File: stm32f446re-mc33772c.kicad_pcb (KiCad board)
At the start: 4 copper layers, 105.3 x 62.5 mm, 120 parts, among them J1 Conn_01x02, J2 USB_B_Micro, J3 Conn_01x03, J4 Conn_01x03, J5 S7B-XH-A, J6 SM06B-GHS-TB, U1 STM32F446RETx, U2 MC33772CTP1AE, U3 LD1086D2M33TR, U4 AMS1117-3.3, U6 LMR51450SDRRR, U7 SN65HVD232, Y1 16MHz

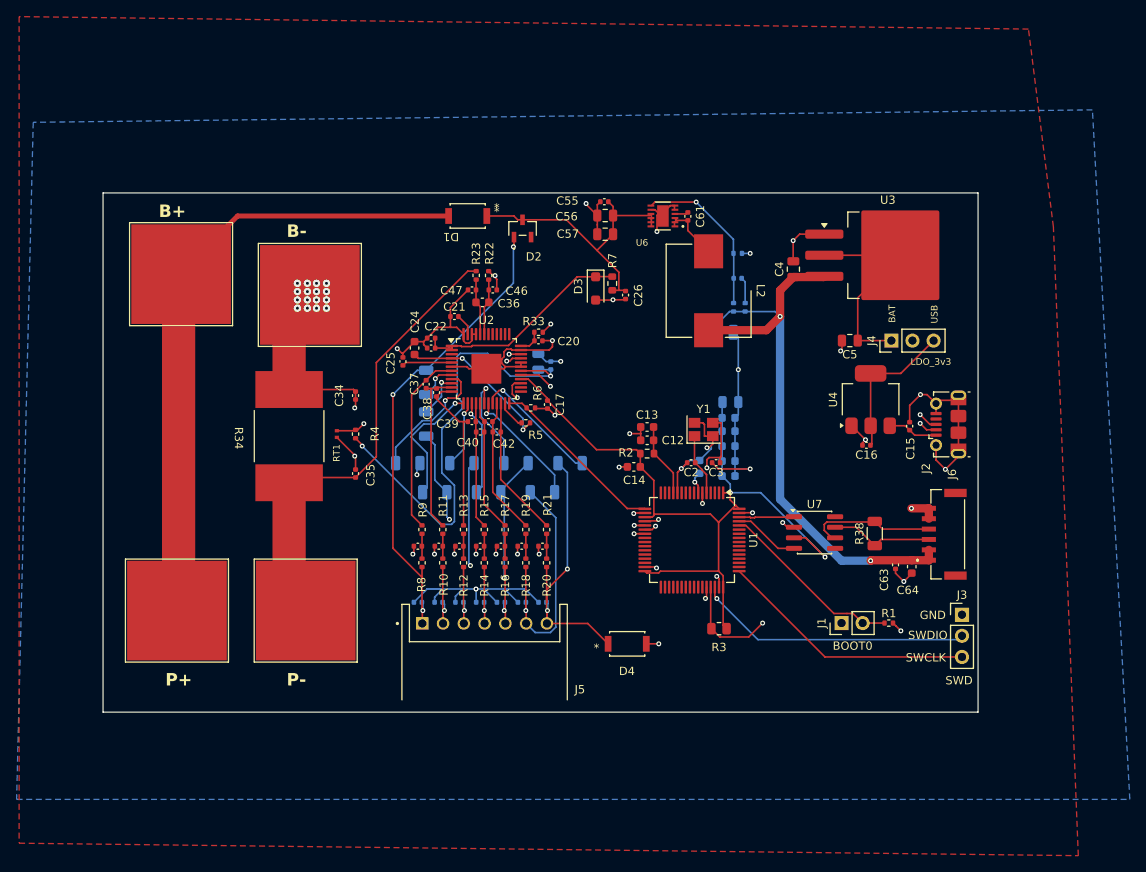
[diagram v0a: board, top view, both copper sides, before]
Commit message: update 3D model
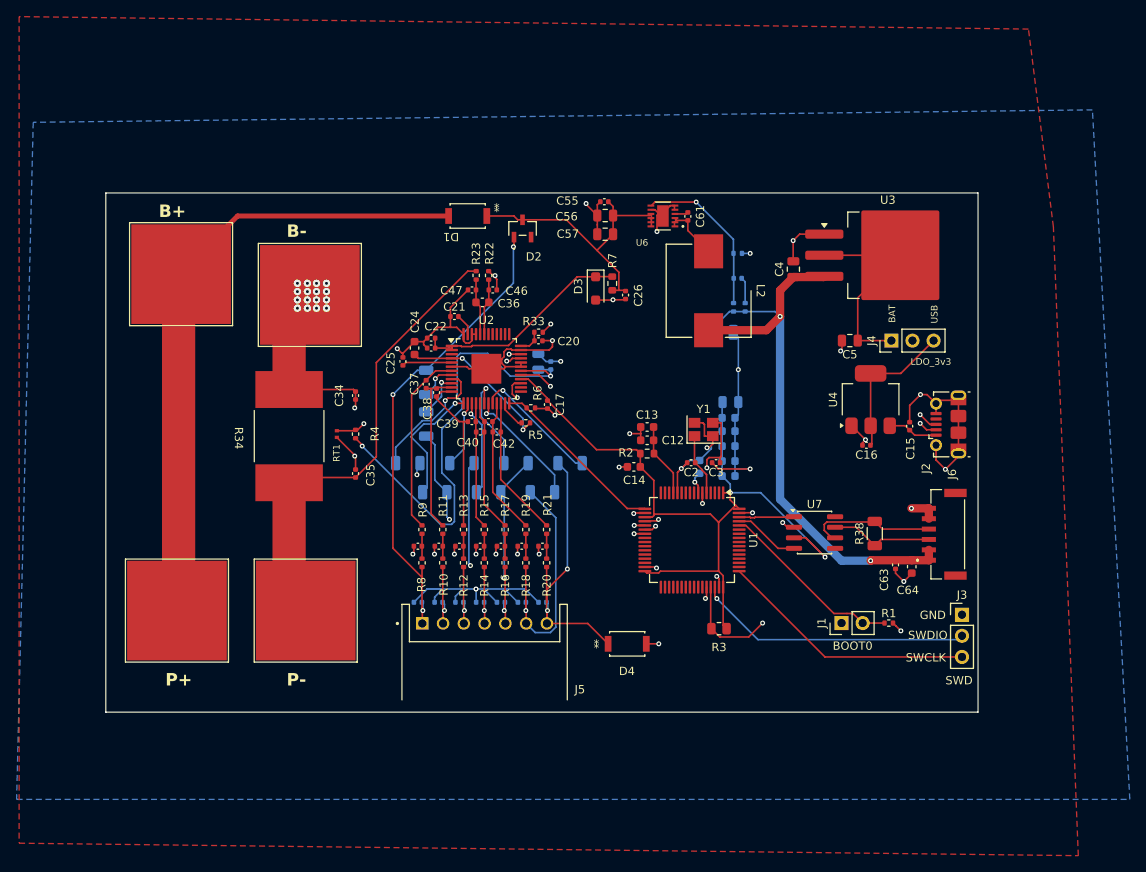
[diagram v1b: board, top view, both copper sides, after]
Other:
- board size 105.3 x 62.5 mm -> 105 x 62.5 mm
- board text removed: "*"
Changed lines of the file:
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@@
 			(outputformat 1)
 			(mirror no)
-			(drillshape 1)
+			(drillshape 0)
 			(scaleselection 1)
-			(outputdirectory "")
+			(outputdirectory "DRL/")
 		)
 	)
@@
 		(sheetname "/STM32F446RE/")
 		(sheetfile "stm32f446re-mc33772c.kicad_sch")
-		(units
-			(unit
-				(name "A")
-				(pins "SH" "5" "1" "3" "2" "4")
-			)
-		)
 		(attr smd)
 		(duplicate_pad_numbers_are_jumpers no)
@@
 		)
 		(embedded_fonts no)
-		(model "${KICAD10_3DMODEL_DIR}/Connector_USB.3dshapes/USB_Micro-B_Molex-105017-0001.step"
+		(model "${KIPRJMOD}/1050170001/1050170001.stp"
 			(offset
-				(xyz 0 0 0)
+				(xyz 0 -1 1)
 			)
 			(scale
@@
 			)
 			(rotate
-				(xyz 0 0 0)
+				(xyz -90 -0 -0)
 			)
 		)
@@
 		(sheetname "/STM32F446RE/")
 		(sheetfile "stm32f446re-mc33772c.kicad_sch")
-		(units
-			(unit
-				(name "A")
-				(pins "1" "2" "3" "4" "5" "6")
-			)
-		)
 		(attr smd)
 		(duplicate_pad_numbers_are_jumpers no)
@@
 		)
 		(embedded_fonts no)
+		(model "${KIPRJMOD}/SM06B_GHS_TB/SM06B-GHS-TB.step"
+			(offset
+				(xyz 0 0 0)
+			)
+			(scale
+				(xyz 1 1 1)
+			)
+			(rotate
+				(xyz -90 -0 -0)
+			)
+		)
 	)
 	(footprint "Capacitor_SMD:C_0402_1005Metric"
@@
 		(sheetname "/STM32F446RE/")
 		(sheetfile "stm32f446re-mc33772c.kicad_sch")
-		(units
-			(unit
-				(name "A")
-				(pins "10" "11" "12" "9" "6" "4" "1" "2" "3" "7" "5" "13" "8")
-			)
-		)
 		(attr smd)
 		(duplicate_pad_numbers_are_jumpers no)
@@
 		)
 		(embedded_fonts no)
+		(model "${KIPRJMOD}/LMR51450SDRRR/DRR0012G.stp"
+			(offset
+				(xyz 0 0 0)
+			)
+			(scale
+				(xyz 1 1 1)
+			)
+			(rotate
+				(xyz 0 0 0)
+			)
+		)
 	)
 	(footprint "MyFootLib:WSLP5931L1000FEA"
@@
 		(sheetname "/POWER/")
 		(sheetfile "power.kicad_sch")
-		(units
-			(unit
-				(name "A")
-				(pins "1" "2")
-			)
-		)
 		(attr smd)
 		(duplicate_pad_numbers_are_jumpers no)
@@
 		)
 		(embedded_fonts no)
+		(model "${KIPRJMOD}/WSLP5931L1000FEA/WSLP5931L1000FEA.step"
+			(offset
+				(xyz 0 0 0)
+			)
+			(scale
+				(xyz 1 1 1)
+			)
+			(rotate
+				(xyz 0 0 0)
+			)
+		)
 	)
 	(footprint "Package_TO_SOT_SMD:SOT-223-3_TabPin2"
@@
 		(sheetname "/POWER/")
 		(sheetfile "power.kicad_sch")
-		(units
-			(unit
-				(name "A")
-				(pins "2" "1")
-			)
-		)
 		(attr smd)
 		(duplicate_pad_numbers_are_jumpers no)
@@
 		)
 		(fp_text user "*"
+			(at -3.7 0 0)
+			(unlocked yes)
+			(layer "F.SilkS")
+			(effects
+				(font
+					(size 1 1)
+					(thickness 0.15)
+				)
+			)
+		)
+		(fp_text user "*"
+			(at -3.7 0.5 0)
+			(layer "F.SilkS")
+			(effects
+				(font
+					(size 1 1)
+					(thickness 0.15)
+				)
+			)
+		)
+		(fp_text user "*"
 			(at -1.7399 0 0)
 			(unlocked yes)
@@
 		)
 		(embedded_fonts no)
+		(model "${KIPRJMOD}/PMEG3050EP_115/SDO_CFP5_SOD128_NEX.iges"
+			(offset
+				(xyz 0 0 0)
+			)
+			(scale
+				(xyz 1 1 1)
+			)
+			(rotate
+				(xyz 0 0 0)
+			)
+		)
 	)
 	(footprint "Capacitor_SMD:C_0402_1005Metric"
@@
 		(sheetname "/POWER/")
 		(sheetfile "power.kicad_sch")
-		(units
-			(unit
-				(name "A")
-				(pins "1" "2" "3" "4" "5" "6" "7")
-			)
-		)
 		(attr through_hole)
 		(duplicate_pad_numbers_are_jumpers no)
@@
 		)
 		(embedded_fonts no)
+		(model "${KIPRJMOD}/S7B_XH_A/S7B-XH-A.step"
+			(offset
+				(xyz 0 0 0)
+			)
+			(scale
+				(xyz 1 1 1)
+			)
+			(rotate
+				(xyz -90 -0 -0)
+			)
+		)
 	)
 	(footprint "Resistor_SMD:R_0402_1005Metric"
@@
 		(sheetname "/POWER/")
 		(sheetfile "power.kicad_sch")
-		(units
-			(unit
-				(name "A")
-				(pins "2" "1")
-			)
-		)
 		(attr smd)
 		(duplicate_pad_numbers_are_jumpers no)
@@
 		)
 		(embedded_fonts no)
+		(model "${KIPRJMOD}/PMEG3050EP_115/SDO_CFP5_SOD128_NEX.iges"
+			(offset
+				(xyz 0 0 0)
+			)
+			(scale
+				(xyz 1 1 1)
+			)
+			(rotate
+				(xyz 0 0 0)
+			)
+		)
 	)
 	(footprint "MyFootLib:L_Wurth_WE-LHMI-1040"
@@
 	)
 	(gr_rect
-		(start 115.1 41.725)
+		(start 115.431914 41.725)
 		(end 220.431914 104.225)
 		(stroke
@@
 		)
 	)
-	(gr_text "*"
-		(at 174.5 96.5 0)
-		(layer "F.SilkS")
-		(effects
-			(font
-				(size 1 1)
-				(thickness 0.15)
-			)
-		)
-	)

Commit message: feat: change B+/P+ to B.Cu and onto one pad
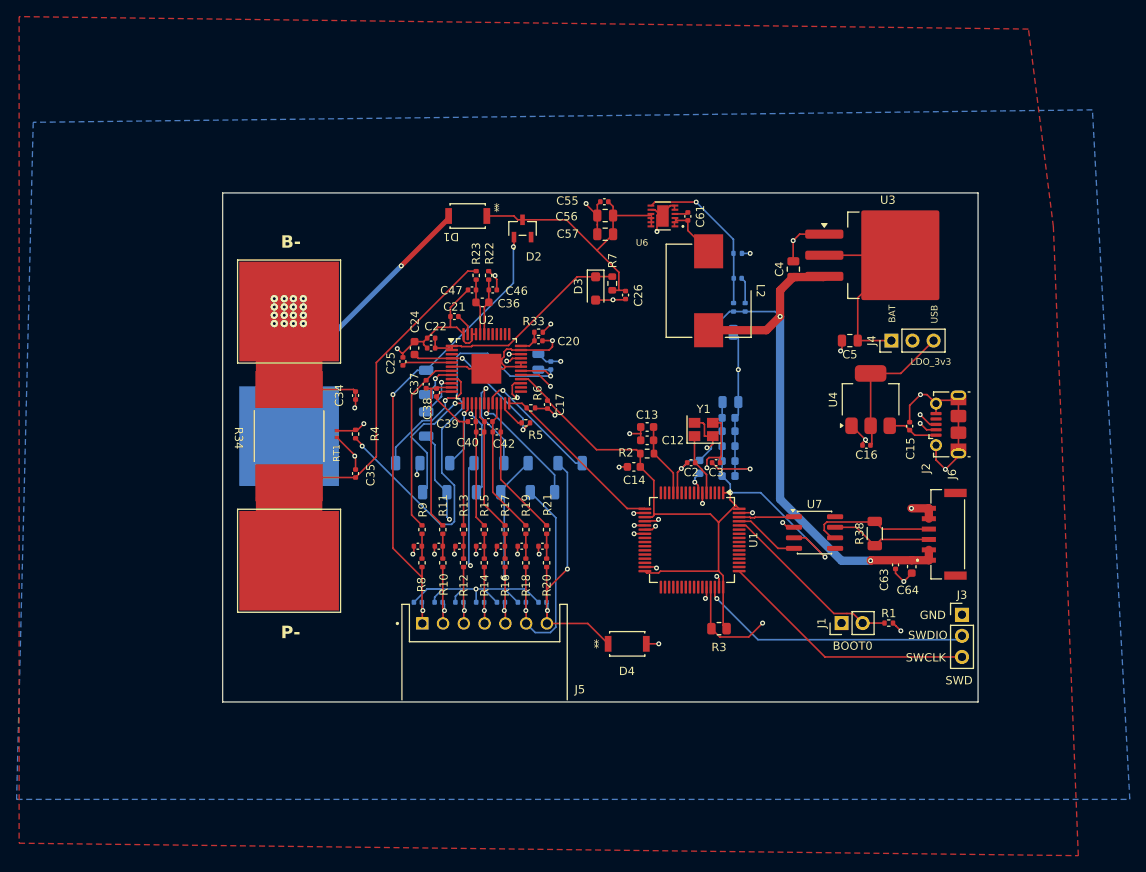
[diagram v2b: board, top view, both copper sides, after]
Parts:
- removed PAD2: pad, MyFootLib:INPUT_PAD
- PAD1: moved to B.Cu
- moved PAD1 23.4 mm to (137.5, 71.0), turned to 180 degrees
- moved PAD4 6.32 mm to (137.5, 86.0)
- moved PAD3 3.20 mm to (137.5, 56.0)
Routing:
- net Pack_24V: track 76.2 -> 34.5 mm, vias 0 -> 1
- net Pack-: track 55.9 -> 42.2 mm
- net Rsense_P: track 220.0 -> 210.1 mm
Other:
- board size 105 x 62.5 mm -> 90.9 x 61.3 mm

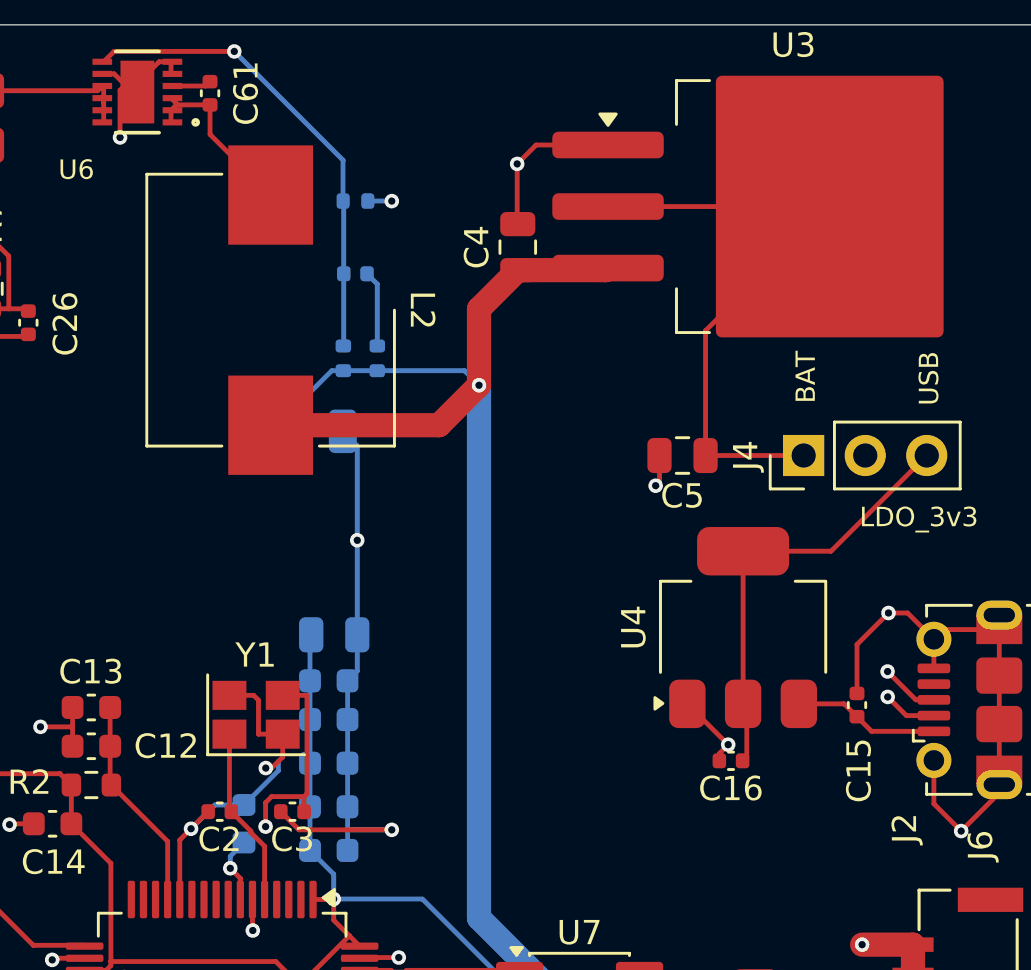
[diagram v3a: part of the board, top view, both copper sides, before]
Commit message: update for JLCPCB with LCSC part #
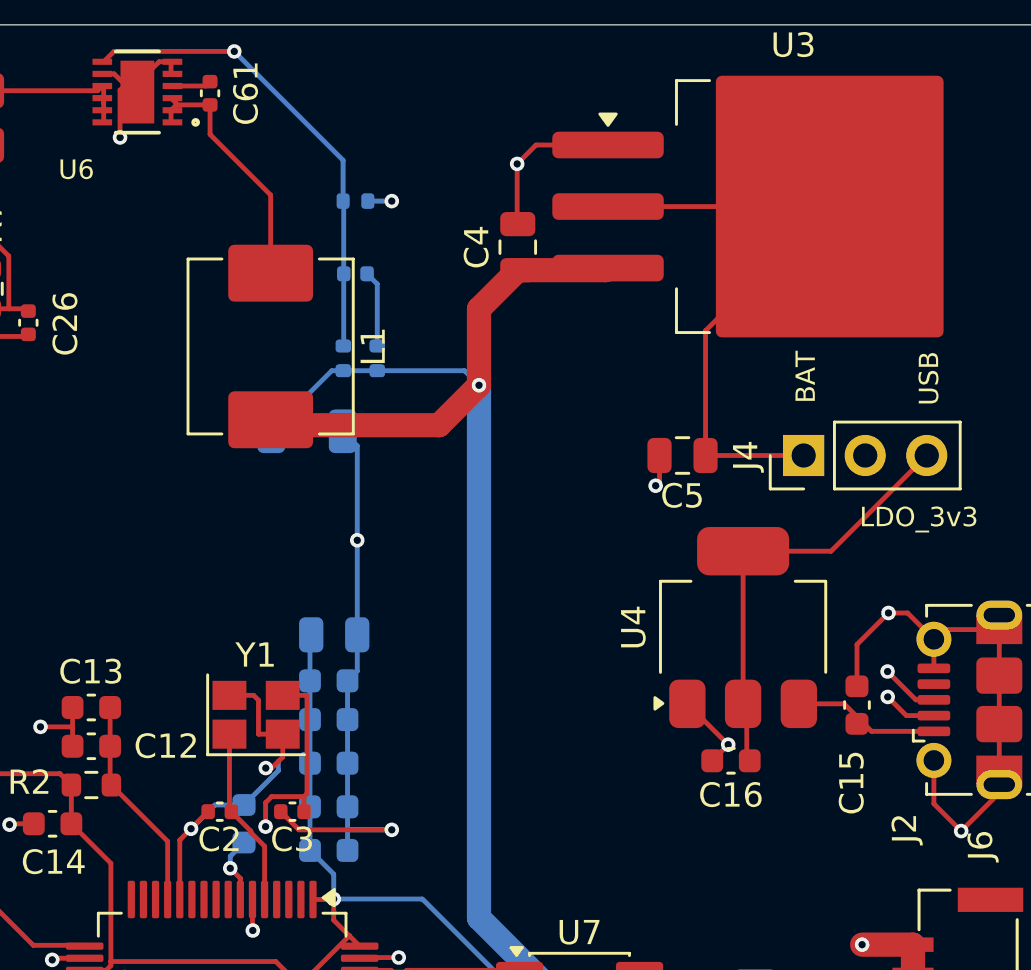
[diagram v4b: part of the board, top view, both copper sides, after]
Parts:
- removed L2: 1040_74437368033, MyFootLib:L_Wurth_WE-LHMI-1040
- added L1: 3.3uH, MyFootLib:PSPMAA0605H-3R3M-ANP, F.Cu at (188.0, 55.0)
- C10, C11, C58, C7, C8, C9: value 100.0n -> 100n
- C15, C16: footprint Capacitor_SMD:C_0402_1005Metric -> Capacitor_SMD:C_0603_1608Metric
- C6: value 10.0u -> 10u
- D3: value BZT52-B39_R1_00001 -> BZT52-C39_R1_00001
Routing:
- net Net-(U6-SW): track 7.33 -> 10.6 mm

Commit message: update PCB for jlcpcb toolkit
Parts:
- C2, C3: value 18p -> 8p
- U1: value STM32F446RETx -> STM32F446RET6

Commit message: export to JLCPCB
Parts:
- C17, C18, C27, C28, C29, C30, C31, C32, C33, C61: value 0.1u -> 100n
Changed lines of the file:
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@@
 			)
 		)
+		(property "FT Rotation Offset" "90"
+			(at 0 0 90)
+			(unlocked yes)
+			(layer "F.Fab")
+			(hide yes)
+			(effects
+				(font
+					(size 1 1)
+					(thickness 0.15)
+				)
+			)
+		)
 		(property ki_fp_filters "Connector*:*_1x??_*")
 		(sheetname "/STM32F446RE/")
@@
 			)
 		)
+		(property "FT Rotation Offset" "90"
+			(at 0 0 90)
+			(unlocked yes)
+			(layer "F.Fab")
+			(hide yes)
+			(effects
+				(font
+					(size 1 1)
+					(thickness 0.15)
+				)
+			)
+		)
 		(property ki_fp_filters "Connector*:*_1x??_*")
 		(sheetname "/STM32F446RE/")
@@
 			)
 		)
-		(property "Value" "0.1u"
+		(property "Value" "100n"
 			(at 0 1.16 0)
 			(layer "F.Fab")
@@
 			)
 		)
+		(property "FT Rotation Offset" "0"
+			(at 0 0 270)
+			(unlocked yes)
+			(layer "F.Fab")
+			(hide yes)
+			(effects
+				(font
+					(size 1 1)
+					(thickness 0.15)
+				)
+			)
+		)
 		(property ki_fp_filters "D?SOD?123F*")
 		(sheetname "/POWER/")
@@
 			)
 		)
-		(property "Value" "0.1u"
+		(property "Value" "100n"
 			(at 0 1.16 0)
 			(layer "F.Fab")
@@
 			)
 		)
-		(property "Value" "0.1u"
+		(property "Value" "100n"
 			(at 0 1.16 0)
 			(layer "F.Fab")
@@
 			)
 		)
-		(property "Value" "0.1u"
+		(property "Value" "100n"
 			(at 0 1.16 0)
 			(layer "F.Fab")
@@
 			)
 		)
+		(property "FT Rotation Offset" "-90"
+			(at 0 0 0)
+			(unlocked yes)
+			(layer "F.Fab")
+			(hide yes)
+			(effects
+				(font
+					(size 1 1)
+					(thickness 0.15)
+				)
+			)
+		)
 		(property ki_fp_filters "SOT-23-3_1P4X3P040_ONS SOT-23-3_1P4X3P040_ONS-M SOT-23-3_1P4X3P040_ONS-L")
 		(sheetname "/POWER/")
@@
 			)
 		)
+		(property "FT Rotation Offset" "90"
+			(at 0 0 0)
+			(unlocked yes)
+			(layer "F.Fab")
+			(hide yes)
+			(effects
+				(font
+					(size 1 1)
+					(thickness 0.15)
+				)
+			)
+		)
 		(property ki_fp_filters "Connector*:*_1x??_*")
 		(sheetname "/STM32F446RE/")
@@
 			)
 		)
+		(property "FT Rotation Offset" "0"
+			(at 0 0 0)
+			(unlocked yes)
+			(layer "F.Fab")
+			(hide yes)
+			(effects
+				(font
+					(size 1 1)
+					(thickness 0.15)
+				)
+			)
+		)
 		(property ki_fp_filters "SDO_CFP5_SOD128_NEX SDO_CFP5_SOD128_NEX-M SDO_CFP5_SOD128_NEX-L")
 		(sheetname "/POWER/")
@@
 			)
 		)
-		(property "Value" "0.1u"
+		(property "Value" "100n"
 			(at 0 1.16 0)
 			(layer "F.Fab")
@@
 			)
 		)
+		(property "FT Rotation Offset" "180"
+			(at 0 0 0)
+			(unlocked yes)
+			(layer "F.Fab")
+			(hide yes)
+			(effects
+				(font
+					(size 1 1)
+					(thickness 0.15)
+				)
+			)
+		)
 		(sheetname "/POWER/")
 		(sheetfile "power.kicad_sch")
@@
 			)
 		)
-		(property "Value" "0.1u"
+		(property "Value" "100n"
 			(at 0 1.16 0)
 			(layer "F.Fab")
@@
 			)
 		)
-		(property "Value" "0.1u"
+		(property "Value" "100n"
 			(at 0 1.16 90)
 			(layer "F.Fab")
@@
 			)
 		)
-		(property "Value" "0.1u"
+		(property "Value" "100n"
 			(at 0 1.16 90)
 			(layer "F.Fab")
@@
 			)
 		)
+		(property "FT Rotation Offset" "0"
+			(at 0 0 180)
+			(unlocked yes)
+			(layer "F.Fab")
+			(hide yes)
+			(effects
+				(font
+					(size 1 1)
+					(thickness 0.15)
+				)
+			)
+		)
 		(property ki_fp_filters "SDO_CFP5_SOD128_NEX SDO_CFP5_SOD128_NEX-M SDO_CFP5_SOD128_NEX-L")
 		(sheetname "/POWER/")
@@
 			)
 		)
-		(property "Value" "0.1u"
+		(property "Value" "100n"
 			(at 0 1.16 0)
 			(layer "F.Fab")
@@
 			)
 		)
-		(property "Value" "0.1u"
+		(property "Value" "100n"
 			(at 0 -1.16 90)
 			(layer "B.Fab")

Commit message: add testpoint
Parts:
- added TP1: TP_SPI_NSS, TestPoint:TestPoint_Pad_D1.0mm, F.Cu at (174.5, 80.0)
- added TP2: TP_SPI_SCK, TestPoint:TestPoint_Pad_D1.0mm, F.Cu at (174.5, 83.6)
- added TP3: TP_SPI_MISO, TestPoint:TestPoint_Pad_D1.0mm, F.Cu at (174.5, 86.6)
- added TP4: TP_SPI_MOSI, TestPoint:TestPoint_Pad_D1.0mm, F.Cu at (174.5, 89.7)
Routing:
- net SPI1_MISO: track 27.5 -> 36.6 mm, vias 2 -> 3
- net SPI1_MOSI: track 31.1 -> 39.9 mm
- net SPI1_SCK: track 33.1 -> 39.7 mm
- net SPI1_NSS: track 30.4 -> 36.7 mm
